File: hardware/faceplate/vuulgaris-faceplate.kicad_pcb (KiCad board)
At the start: 4 copper layers, 298.3 x 137.8 mm, 54 parts, among them J1 HX JN2.54-2x5P TP H8.9, U1 MSP430FR2675TPT, Y1 32.768kHz FC-135 12.5pF

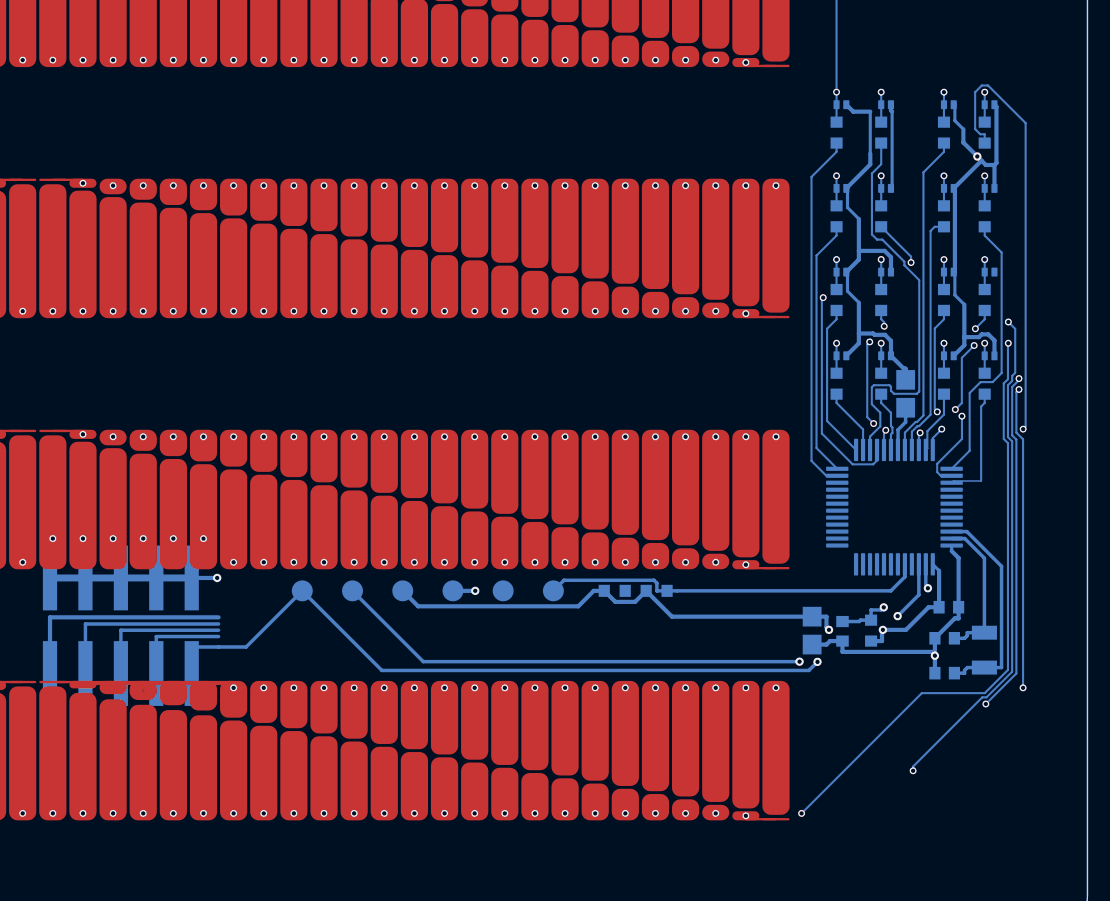
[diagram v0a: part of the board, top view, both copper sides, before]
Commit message: faceplate: rebuildable from zero; J1 corridor scripted; 10 open
The board now rebuilds from its scripts: mkroute --unroute, then
mkplace --force, mkpads, mkbuses, mkcells, mkescape, mkzones, mkroute.
mkescape draws J1's escape and the whole corridor: five lines fanned to
1.3mm (RXD straight, the rest diverging from it; TXD bends after 3V3),
each test pad ON its own line, R2 across the 3V3 and TXD lines, TP4 to
J1's GND via, J1's GND row link (was mkboard's). R3 moved to the margin
beside U1 pin 5. The L3 strip now lies under all five lines, 0.75 clear
of both pads. mkzones builds new zones before removing old ones (KiCad
7 bindings: Outline() opaque after a removal; a Python-built outline
crashes pcbnew).

Open after Freerouting: GND 3, MSP430_RXD 1, MSP430_TXD 1, PAD3_RX0 1, PAD3_RX1 1, PAD3_RX3 1, PAD4_RX0 1, PAD4_RX1 1.
Checked: DRC --unrouted 0 errors (full DRC: the 10 unconnected only);
boardcheck clearance 0, parity 0; panelcheck --strict 17 OK.
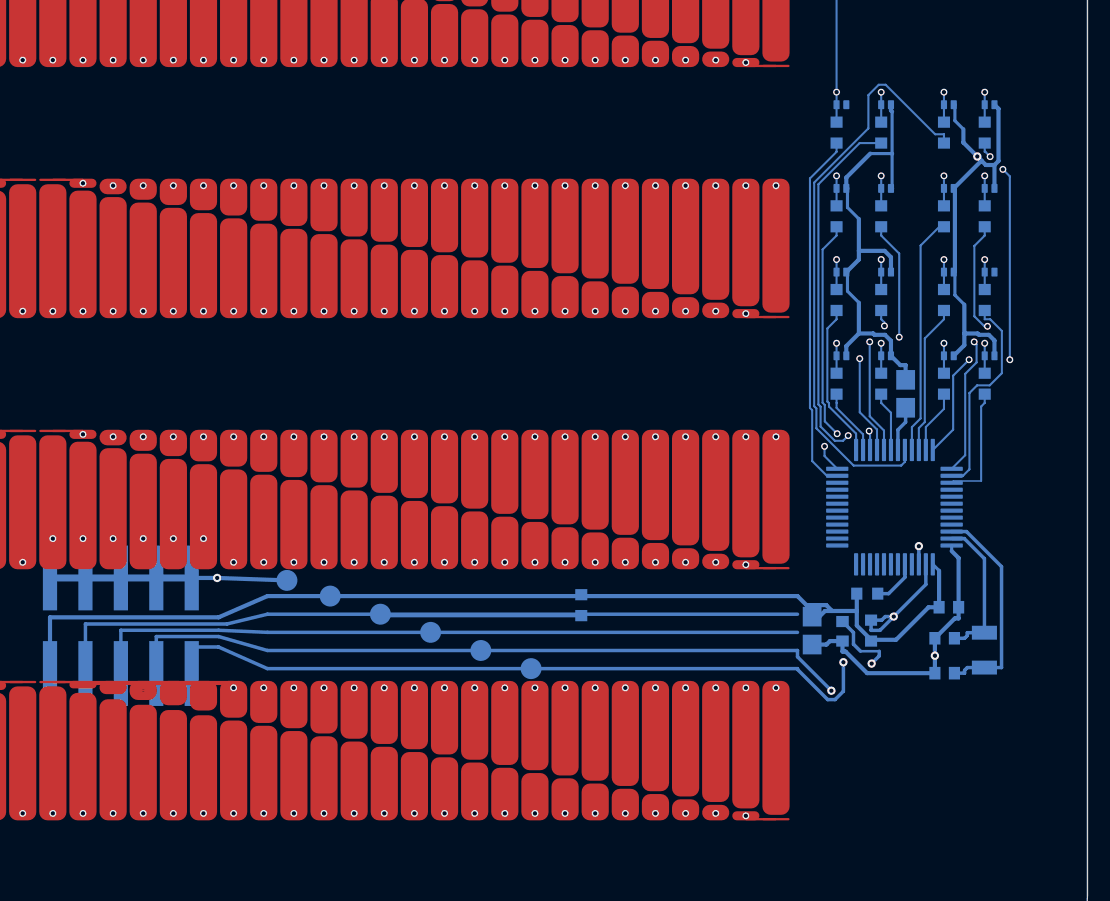
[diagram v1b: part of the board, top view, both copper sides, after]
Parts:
- moved TP1 17.3 mm to (358.4, 165.6)
- moved R3 15.1 mm to (382.5, 160.2)
- moved TP4 11.9 mm to (340.9, 159.2)
- moved TP2 10.1 mm to (354.8, 164.3)
- moved TP6 9.29 mm to (351.2, 163.0)
- moved TP5 8.96 mm to (347.6, 161.7)
- moved TP3 5.21 mm to (344.0, 160.4)
- moved R2 2.61 mm to (362.0, 161.0), turned to -90 degrees
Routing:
- net /MSP430_TXD: track 13.1 -> 69.1 mm
- net /PAD4_RX1: track 272.2 -> 218.4 mm, vias 51 -> 49
- net /PAD4_RX0: track 271.6 -> 219.6 mm, vias 46 -> 44
- net /CAP2.0: track 23.2 -> 41.8 mm
- net /PAD3_RX2: track 162.7 -> 180.4 mm
- net /MSP430_RXD: track 37.6 -> 55.0 mm
- net /PAD2_RX3: track 108.3 -> 125.5 mm
- net /MSP_RST: track 59.3 -> 74.7 mm
- net /PAD4_RX2: track 207.0 -> 192.4 mm, vias 51 -> 49
- net /P3V3_MSP430: track 63.3 -> 77.3 mm, vias 2 -> 0
- net /PAD3_RX0: track 233.5 -> 219.8 mm
- net /CAP3.0: track 38.7 -> 26.8 mm, vias 2 -> 4
- net /CAP1.1: track 26.3 -> 19.0 mm
- net /PAD4_RX3: track 152.8 -> 150.2 mm, vias 51 -> 49
- net /GND: track 101.8 -> 102.7 mm, vias 4 -> 3
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
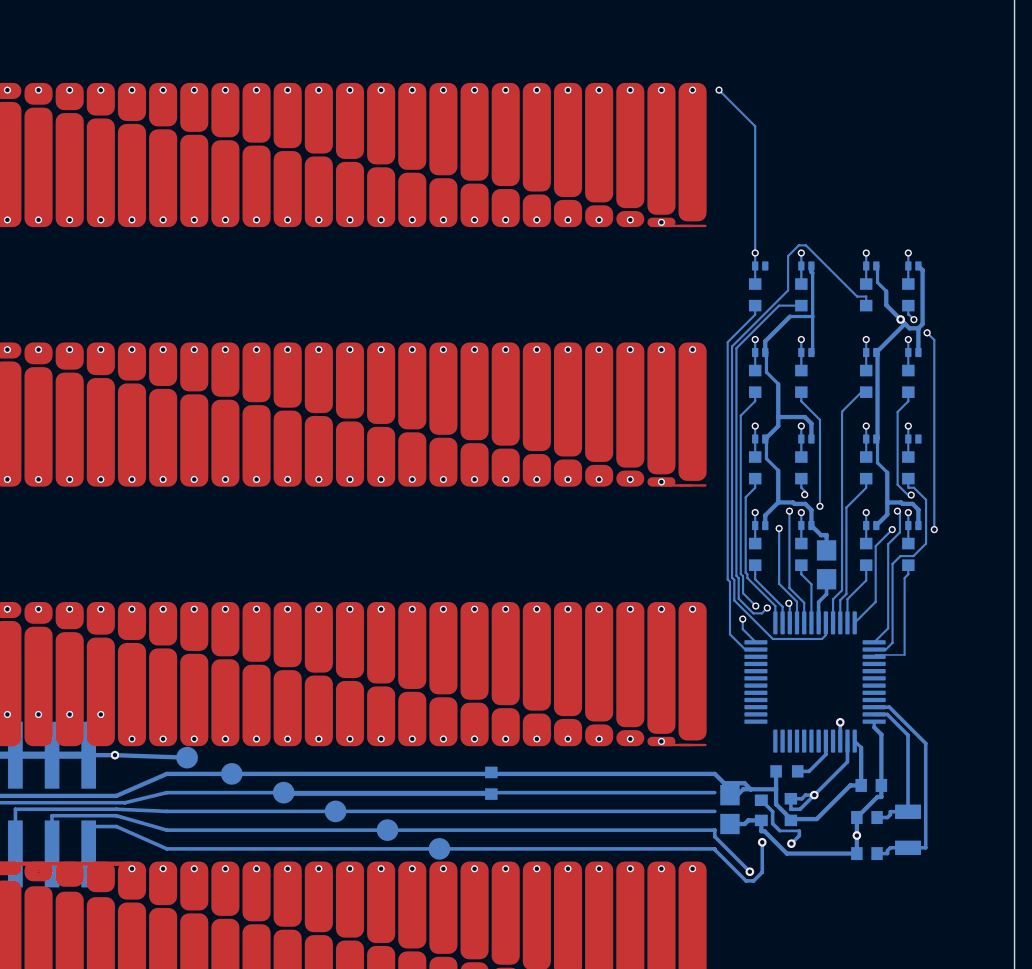
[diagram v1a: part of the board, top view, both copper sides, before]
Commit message: faceplate: fully routed -- DRC 0 errors, 0 unconnected
Everything a router kept fumbling is now drawn by script, and the board
rebuilds from zero and closes on the first Freerouting pass.

- mkfanin.py (new): the L2 fan-in, every bus exit to its cell via, drawn
  exactly. Pads 1-3 come in from a left strip, pad 4 from a right strip;
  each cell's via sits at its own height in the order its pad's lines
  arrive, so no line crosses another.
- mkcells.py: vias staggered to match (VIA_X / VIA_LEVEL), TVS grounds
  (GND via beside pin 2, one sent up between rows, C3 tied to row 4 col 1).
- mkescape.py: RXD and TXD hop to R3 / U1 pin 4 on L2; J1 GND stub from the
  pad centre (the old one left a 10um sliver).
- mkplace.py: C1 out of the corridor mouth, where it blocked RST/TXD/RXD.
- mkroute.py: prune (free-ended and sub-20um segments) and stitch (a GND
  via + straight stub for any B.Cu GND pad the plane does not reach).
- mkzones.py: L3 plane solid, not hatched -- a via in a hatch hole touched
  nothing. Still only in the margin and corridor, never under a pad.
- mkbuses.py: every via on a segment end; exits dead level into the margin.
- boardcheck.py: every In2 zone is a plane node, overlapping same-net zones
  join. Main board unchanged: 0 broken, 0 clearance, parity 944.

Checked: netcheck 145/145; boardcheck 0 broken, 0 clearance, 0 degenerate;
KiCad DRC 0 errors, 0 unconnected (31 library pin-1 silk warnings);
panelcheck --strict 17 OK, nothing on F.Cu, nothing under a pad but its own
nets. Main board DRC 0 errors, place.py all 24.
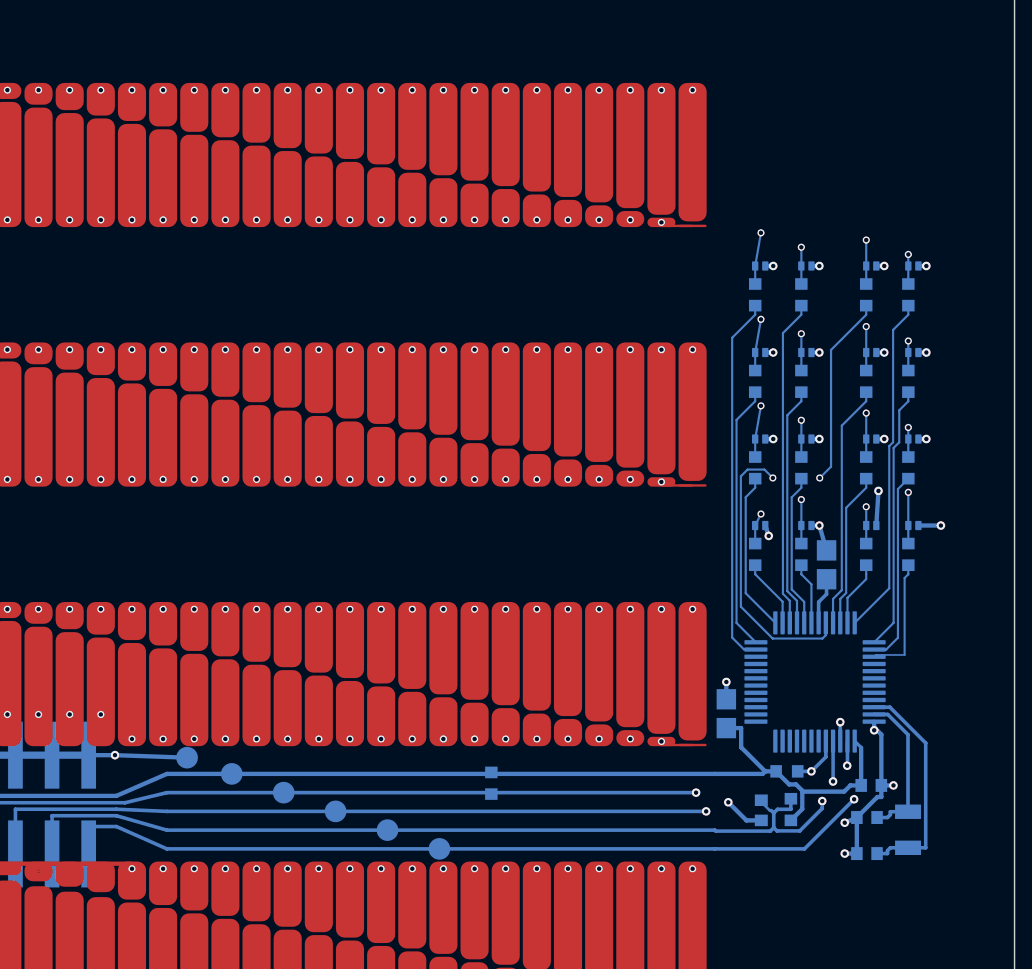
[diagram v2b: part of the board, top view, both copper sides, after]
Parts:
- moved C1 6.65 mm to (378.3, 156.2), turned to 90 degrees
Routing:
- net /PAD4_RX1: track 218.4 -> 274.5 mm
- net /GND: track 102.7 -> 48.1 mm, vias 3 -> 23
- net /PAD4_RX0: track 219.6 -> 268.9 mm
- net /PAD3_RX3: track 118.5 -> 152.5 mm
- net /PAD3_RX1: track 218.4 -> 244.1 mm
- net /PAD3_RX0: track 219.8 -> 238.2 mm
- net /PAD4_RX2: track 192.4 -> 207.0 mm
- net /PAD4_RX3: track 150.2 -> 160.5 mm
- net /MSP430_RXD: track 55.0 -> 64.5 mm, vias 0 -> 2
- net /PAD3_RX2: track 180.4 -> 188.2 mm
- net /MSP_RST: track 74.7 -> 67.3 mm, vias 3 -> 2
- net /CAP1.0: track 28.7 -> 22.7 mm, vias 2 -> 0
- net /PAD1_RX2: track 177.4 -> 183.4 mm
- net /CAP2.0: track 41.8 -> 36.0 mm, vias 0 -> 2
- net /PAD2_RX3: track 125.5 -> 130.3 mm
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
